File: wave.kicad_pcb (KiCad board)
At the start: 4 copper layers, 60 x 60 mm, 129 parts, among them J101 CORTEX-DEBUG, J102 WAGO-2065, J103 WAGO-2065, J104 WAGO-2065, J105 WAGO-2065, J106 WAGO-2065, J107 WAGO-2065, J301 2x05_Horizontal, J401 2x05_Horizontal, J501 WAGO-2065, J502 WAGO-2065, Q201 IRF9358, SW101 SW_Push, SW102 SW_Push, U101 TPS78433QWDRBRQ1, U102 ATSAMD51J, U201 MA12070P, U301 SN65MLVD203B, U401 SN65MLVD203B, U501 74AHC1G125, Y101 32k768

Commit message: Refresh
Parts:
- added ICON110: Dot, V2_Artwork:Dot_Small, F.Cu at (77.8, 57.0)
- added ICON111: Plug, V2_Artwork:Plug_Small, F.Cu at (73.5, 113.8)
- added ICON112: Socket, V2_Artwork:Socket_Small, F.Cu at (120.5, 113.8)
- R103, R104: value 5k1 -> 2k7
- moved ICON104 0.25 mm to (69.2, 57.0)

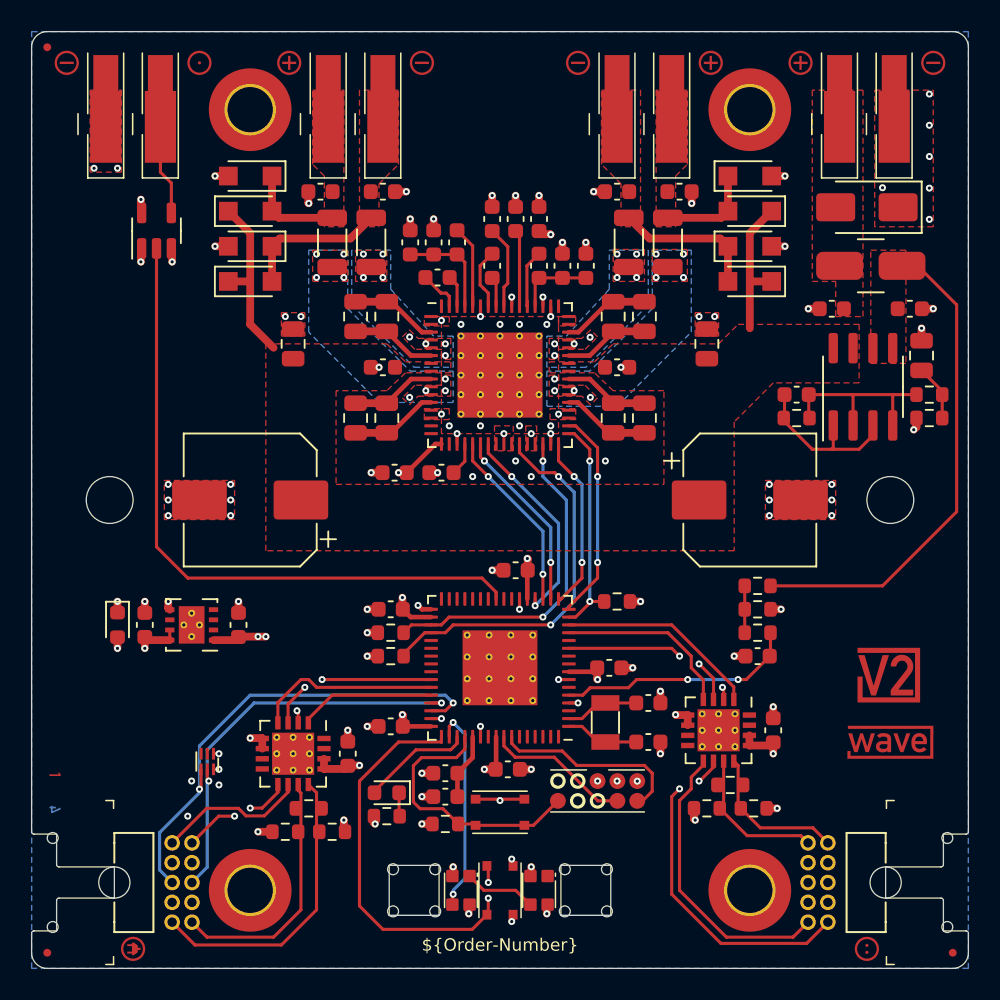
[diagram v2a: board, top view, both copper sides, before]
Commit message: Replace icons
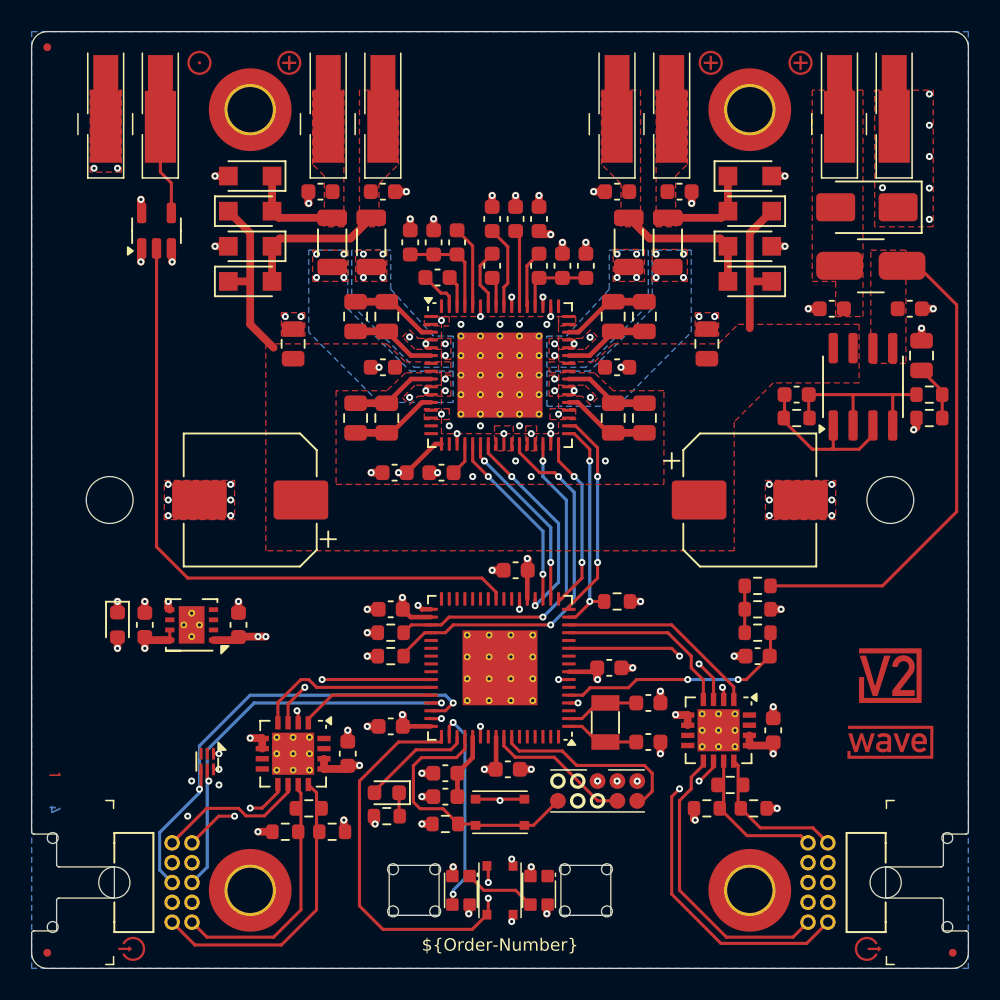
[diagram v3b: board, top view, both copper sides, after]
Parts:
- removed ICON104, ICON106: Minus, V2_Artwork:Minus_Small
- removed ICON111: Plug, V2_Artwork:Plug_Small
- removed ICON112: Socket, V2_Artwork:Socket_Small
- ICON101: value Minus -> Arrow_In; footprint V2_Artwork:Minus_Small -> V2_Artwork:Arrow_In
- ICON102: value Minus -> Arrow_Out; footprint V2_Artwork:Minus_Small -> V2_Artwork:Arrow_Out
- U101: value TPS78433QWDRBRQ1 -> TPS78433QWDRBRQ1
- moved ICON101 59.7 mm to (73.5, 113.8)
- moved ICON102 59.7 mm to (120.5, 113.8)

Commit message: Refresh
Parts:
- removed the C102 at (93.5, 102.5)
- removed the R301 at (86.2, 106.2)
- removed R303, R403: 10k, Resistor_SMD:R_0603_1608Metric
- removed the R401 at (113.2, 104.8)
- U301, U401: value SN65MLVD203B -> THVD24x2; footprint V2_Package_DFN_QFN:WQFN-16-1EP_4x4mm_P0.65mm_EP2.7x2.7mm_ThermalVias -> V2_Package_SON:VSON-10-4-1EP_3x3mm_P0.5mm_EP1.65x2.4mm_ThermalVias
- moved ICON103 2.76 mm to (70.8, 113.5)
- moved ICON106 2.76 mm to (123.2, 113.5)
- moved C101 1.75 mm to (93.5, 102.2)
- moved C107 1.50 mm to (75.8, 93.0)
- moved C108 1.50 mm to (81.8, 93.0)
- moved TVS101 1.50 mm to (74.0, 93.0)
- moved U101 1.50 mm to (78.8, 93.0)
- moved R301 0.75 mm to (84.0, 104.8)
- moved C301 0.50 mm to (86.8, 101.2)
- moved C401 0.50 mm to (114.0, 99.8)
- moved R401 0.50 mm to (111.2, 103.2)
- moved U501 0.50 mm to (75.5, 67.8)
- renumbered C103 to C102, C104 to C103, C105 to C104, C106 to C105, C107 to C106, C108 to C107, C109 to C108, C110 to C109, C111 to C110, C112 to C111, C113 to C112, C114 to C113, C233 to C207, C207 to C208, C208 to C209, C232 to C210, C209 to C211, C210 to C212, C211 to C213, C212 to C214, C213 to C215, C214 to C216, C215 to C217, C216 to C218, C217 to C219, C218 to C220, C219 to C221, C220 to C222, C221 to C223, C222 to C224, C223 to C225, C224 to C226, C225 to C227, C226 to C228, C227 to C229, C228 to C230, C229 to C231, C230 to C232, C231 to C233, ICON103 to ICON101, ICON107 to ICON102, ICON101 to ICON103, ICON105 to ICON104, ICON110 to ICON105, ICON102 to ICON106, ICON108 to ICON107, ICON109 to ICON108, R302 to R301, R402 to R401
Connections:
- U301 pad 10: /Link Plug/TX-Z -> +3V3
- U301 pad 11: /Link Plug/RX-B -> GND
- U301 pad 6: GND -> /Link Plug/TX-Y
- U301 pad 7: unconnected-(U301-Pad7) -> /Link Plug/TX-Z
- U301 pad 8: unconnected-(U301-Pad8) -> /Link Plug/RX-B
- U301 pad 9: /Link Plug/TX-Y -> /Link Plug/RX-A
- U401 pad 10: /Link Socket/TX-Z -> +3V3
- U401 pad 11: /Link Socket/RX-B -> GND
- U401 pad 6: GND -> /Link Socket/TX-Y
- U401 pad 7: unconnected-(U401-Pad7) -> /Link Socket/TX-Z
- U401 pad 8: unconnected-(U401-Pad8) -> /Link Socket/RX-B
- U401 pad 9: /Link Socket/TX-Y -> /Link Socket/RX-A
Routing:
- net +3V3: track 27.6 -> 22.8 mm, vias 17 -> 15
- net +5V: track 12.4 -> 8.62 mm
- net GND: track 48.7 -> 46.2 mm, vias 109 -> 102
- net /VDDCORE: track 3.99 -> 2.62 mm
- net /Link Plug/RX-B: track 16.2 -> 17.1 mm
- net /RESET: track 17.4 -> 16.6 mm
- net /Socket-TX: track 11.6 -> 12.3 mm
- net /Socket-TX-Enable: track 11.4 -> 12.0 mm
- net /LED-Data: track 42.5 -> 43.1 mm
- net /Socket-RX: track 13.0 -> 13.5 mm
- net /Link Plug/TX-Z: track 9.66 -> 9.46 mm, vias 0 -> 2
- net /Link Plug/TX-Y: track 7.34 -> 7.54 mm, vias 2 -> 0
- added copper zone on F.Cu, net +3V3
- added copper zone on F.Cu, net +5V
- added copper zone on In2.Cu, net GND
